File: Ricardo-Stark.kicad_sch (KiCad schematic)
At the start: 49 parts, among them J1 RBUS, U1 ESP32-S3, Y1 R940000171

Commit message: Commit
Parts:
- removed ArcReactorCore1, Eye1, Eye2: Blue_LED, Resistor_SMD:R_0402_1005Metric, symbol Device:LED_Small
- removed R11, R12, R13: 1k, Resistor_SMD:R_0402_1005Metric, symbol Device:R_Small
- removed R14: 3k, Resistor_SMD:R_0402_1005Metric, symbol Device:R_Small
- removed Repulsor1, Repulsor2: White_LED, Resistor_SMD:R_0402_1005Metric, symbol Device:LED_Small
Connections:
- net BUCKC_EN: no longer U1.17 (GPIO12/ADC2_CH1)
- net VSPI_MISO: now also U1.44 (MTCK/JTAG/GPIO39); no longer U1.21 (GPIO15/ADC2_CH4/XTAL_32K_P)
- net VSPI_MOSI: now also U1.47 (MTDI/JTAG/GPIO41); no longer U1.45 (MTDO/JTAG/GPIO40)
- net VSPI_SCLK: now also U1.45 (MTDO/JTAG/GPIO40); no longer U1.47 (MTDI/JTAG/GPIO41)
- net GPIO0 renamed GPIO9
- net GPIO1 renamed GPIO7
- net GPIO2 renamed GPIO8
- net GPIO3 renamed GPIO6
- no-connect marks 17 -> 18
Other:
- sheet actuators ports: added GPIO4, GPIO5, GPIO6, GPIO7, GPIO8, GPIO9; removed none
- sheet microSD ports: added SD1_CS, VSPI_MISO, VSPI_MOSI, VSPI_SCLK; removed none

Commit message: commit
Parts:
- added 3V3LED10: PURPLE_LED, LED_SMD:LED_0402_1005Metric, symbol Device:LED_Small
- added 3V3LED2, 3V3LED3, 3V3LED4, 3V3LED8: BLUE_LED, LED_SMD:LED_0402_1005Metric, symbol Device:LED_Small
- added 3V3LED5: ORANGE_LED, LED_SMD:LED_0402_1005Metric, symbol Device:LED_Small
- added 3V3LED6: RED_LED, LED_SMD:LED_0402_1005Metric, symbol Device:LED_Small
- added 3V3LED7: YELLOW_LED, LED_SMD:LED_0402_1005Metric, symbol Device:LED_Small
- added 3V3LED9: GREEN_LED, LED_SMD:LED_0402_1005Metric, symbol Device:LED_Small
- added JP31: SolderJumper_2_Open, iclr:SmallerSolderJP, symbol Jumper:SolderJumper_2_Open
- added R11, R12, R13, R44: 470, Resistor_SMD:R_0402_1005Metric, symbol Device:R_Small
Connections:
- net +3V3: now also JP31.2 (B), R11.2, R12.2, R44.2
- net GND: now also 3V3LED10.1 (K), 3V3LED2.1 (K), 3V3LED3.1 (K), 3V3LED4.1 (K), 3V3LED5.1 (K), 3V3LED6.1 (K), 3V3LED7.1 (K), 3V3LED8.1 (K), 3V3LED9.1 (K)
- net Servo1PWM: now also U1.17 (GPIO12/ADC2_CH1); no longer U1.16 (GPIO11/ADC2_CH0)
- net Servo2PWM: now also U1.16 (GPIO11/ADC2_CH0); no longer U1.15 (GPIO10/ADC1_CH9)
- net SD_EN: now reaches U1.43 (GPIO38)
- new net: 3V3LED10.2 (A), 3V3LED4.2 (A), 3V3LED5.2 (A), 3V3LED6.2 (A), 3V3LED7.2 (A), 3V3LED9.2 (A), JP31.1 (A), R13.1
- new net: 3V3LED2.2 (A), R11.1
- new net: 3V3LED8.2 (A), R44.1
- new net: 3V3LED3.2 (A), R12.1
- new net LEDC: R13.2, U1.15 (GPIO10/ADC1_CH9)
- no-connect marks 18 -> 16
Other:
- sheet microSD ports: added SD_Pow; removed none

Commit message: 5v breakout
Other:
- sheet actuators ports: added 5V; removed none
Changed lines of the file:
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@@
 	(wire
 		(pts
-			(xy 213.36 58.42) (xy 219.71 58.42)
+			(xy 218.44 58.42) (xy 224.79 58.42)
 		)
 		(stroke
@@
 	(wire
 		(pts
-			(xy 213.36 54.61) (xy 219.71 54.61)
+			(xy 218.44 54.61) (xy 224.79 54.61)
 		)
 		(stroke
@@
 	(wire
 		(pts
+			(xy 187.96 64.008) (xy 180.34 64.008)
+		)
+		(stroke
+			(width 0)
+			(type default)
+		)
+	)
+	(wire
+		(pts
 			(xy 55.88 127) (xy 69.85 127)
 		)
@@
 	(wire
 		(pts
-			(xy 213.36 62.23) (xy 219.71 62.23)
+			(xy 218.44 62.23) (xy 224.79 62.23)
 		)
 		(stroke
@@
 	)
 	(label "Servo1PWM"
-		(at 219.71 58.42 0)
+		(at 224.79 58.42 0)
 		(fields_autoplaced yes)
 		(effects
@@
 	)
 	(label "GPIO7"
-		(at 182.88 53.848 180)
+		(at 187.96 53.848 180)
 		(fields_autoplaced yes)
 		(effects
@@
 	)
 	(label "GPIO6"
-		(at 182.88 51.562 180)
+		(at 187.96 51.562 180)
 		(fields_autoplaced yes)
 		(effects
@@
 	)
 	(label "Servo2PWM"
-		(at 219.71 54.61 0)
+		(at 224.79 54.61 0)
 		(fields_autoplaced yes)
 		(effects
@@
 	)
 	(label "GPIO9"
-		(at 182.88 62.484 180)
+		(at 187.96 62.484 180)
 		(fields_autoplaced yes)
 		(effects
@@
 	)
 	(label "GPIO4"
-		(at 182.88 56.134 180)
+		(at 187.96 56.134 180)
 		(fields_autoplaced yes)
 		(effects
@@
 	)
 	(label "ServoV_LOG"
-		(at 219.71 62.23 0)
+		(at 224.79 62.23 0)
 		(fields_autoplaced yes)
 		(effects
@@
 	)
 	(label "GPIO8"
-		(at 182.88 60.452 180)
+		(at 187.96 60.452 180)
 		(fields_autoplaced yes)
 		(effects
@@
 	)
 	(label "GPIO5"
-		(at 182.88 58.166 180)
+		(at 187.96 58.166 180)
 		(fields_autoplaced yes)
 		(effects
@@
 	)
 	(symbol
+		(lib_id "power:+5V")
+		(at 180.34 64.008 180)
+		(unit 1)
+		(exclude_from_sim no)
+		(in_bom yes)
+		(on_board yes)
+		(dnp no)
+		(fields_autoplaced yes)
+		(property "Reference" "#PWR092"
+			(at 180.34 60.198 0)
+			(effects
+				(font
+					(size 1.27 1.27)
+				)
+				(hide yes)
+			)
+		)
+		(property "Value" "+5V"
+			(at 180.34 69.088 0)
+			(effects
+				(font
+					(size 1.27 1.27)
+				)
+			)
+		)
+		(property "Footprint" ""
+			(at 180.34 64.008 0)
+			(effects
+				(font
+					(size 1.27 1.27)
+				)
+				(hide yes)
+			)
+		)
+		(property "Datasheet" ""
+			(at 180.34 64.008 0)
+			(effects
+				(font
+					(size 1.27 1.27)
+				)
+				(hide yes)
+			)
+		)
+		(property "Description" ""
+			(at 180.34 64.008 0)
+			(effects
+				(font
+					(size 1.27 1.27)
+				)
+				(hide yes)
+			)
+		)
+		(pin "1"
+		)
+		(instances
+			(project "Ricardo-Stark"
+				(path "/7db990e4-92e1-4f99-b4d2-435bbec1ba83"
+					(reference "#PWR092")
+					(unit 1)
+				)
+			)
+		)
+	)
+	(symbol
 		(lib_id "power:+3.3V")
 		(at 59.69 142.24 0)
@@
 	)
 	(sheet
-		(at 182.88 49.53)
+		(at 187.96 49.53)
 		(size 30.48 15.24)
 		(fields_autoplaced yes)
@@
 		)
 		(property "Sheetname" "actuators"
-			(at 182.88 48.8184 0)
+			(at 187.96 48.8184 0)
 			(effects
 				(font
@@
 		)
 		(property "Sheetfile" "actuators.kicad_sch"
-			(at 182.88 65.3546 0)
+			(at 187.96 65.3546 0)
 			(effects
 				(font
@@
 		)
 		(pin "SERVO2" bidirectional
-			(at 213.36 54.61 0)
+			(at 218.44 54.61 0)
 			(effects
 				(font
@@
 		)
 		(pin "SERVO1" bidirectional
-			(at 213.36 58.42 0)
+			(at 218.44 58.42 0)
 			(effects
 				(font
@@
 		)
 		(pin "SERVO_LOG" output
-			(at 213.36 62.23 0)
+			(at 218.44 62.23 0)
 			(effects
 				(font
@@
 		)
 		(pin "GPIO6" input
-			(at 182.88 51.562 180)
+			(at 187.96 51.562 180)
 			(effects
 				(font
@@
 		)
 		(pin "GPIO7" input
-			(at 182.88 53.848 180)
+			(at 187.96 53.848 180)
 			(effects
 				(font
@@
 		)
 		(pin "GPIO4" input
-			(at 182.88 56.134 180)
+			(at 187.96 56.134 180)
 			(effects
 				(font
@@
 		)
 		(pin "GPIO5" input
-			(at 182.88 58.166 180)
+			(at 187.96 58.166 180)
 			(effects
 				(font
@@
 		)
 		(pin "GPIO8" input
-			(at 182.88 60.452 180)
+			(at 187.96 60.452 180)
 			(effects
 				(font
@@
 		)
 		(pin "GPIO9" input
-			(at 182.88 62.484 180)
+			(at 187.96 62.484 180)
+			(effects
+				(font
+					(size 1.27 1.27)
+				)
+				(justify left)
+			)
+		)
+		(pin "5V" output
+			(at 187.96 64.008 180)
 			(effects
 				(font

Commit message: review changes
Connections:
- net Fuse_Cont: now reaches U1.19 (GPIO14/ADC2_CH3)
- no-connect marks 16 -> 15
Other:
- sheet Pyro ports: added Fuse_Cont; removed none
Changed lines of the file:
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@@
 	)
 	(no_connect
-		(at 69.85 105.41)
-	)
-	(no_connect
 		(at 135.89 87.63)
 	)
@@
 	(wire
 		(pts
+			(xy 207.264 134.874) (xy 214.884 134.874)
+		)
+		(stroke
+			(width 0)
+			(type default)
+		)
+	)
+	(wire
+		(pts
 			(xy 143.51 138.43) (xy 156.21 138.43)
 		)
@@
 		)
 	)
+	(label "Fuse_Cont"
+		(at 69.85 105.41 180)
+		(fields_autoplaced yes)
+		(effects
+			(font
+				(size 1.27 1.27)
+			)
+			(justify right bottom)
+		)
+	)
 	(label "VSPI_MISO"
 		(at 69.85 118.11 180)
@@
 		)
 	)
+	(label "Fuse_Cont"
+		(at 207.264 134.874 180)
+		(fields_autoplaced yes)
+		(effects
+			(font
+				(size 1.27 1.27)
+			)
+			(justify right bottom)
+		)
+	)
 	(label "CAN-"
 		(at 115.57 25.4 270)
@@
 			(effects
 				(font
+					(size 1.27 1.27)
+				)
+				(justify left)
+			)
+		)
+		(pin "Fuse_Cont" output
+			(at 214.884 134.874 180)
+			(effects
+				(font

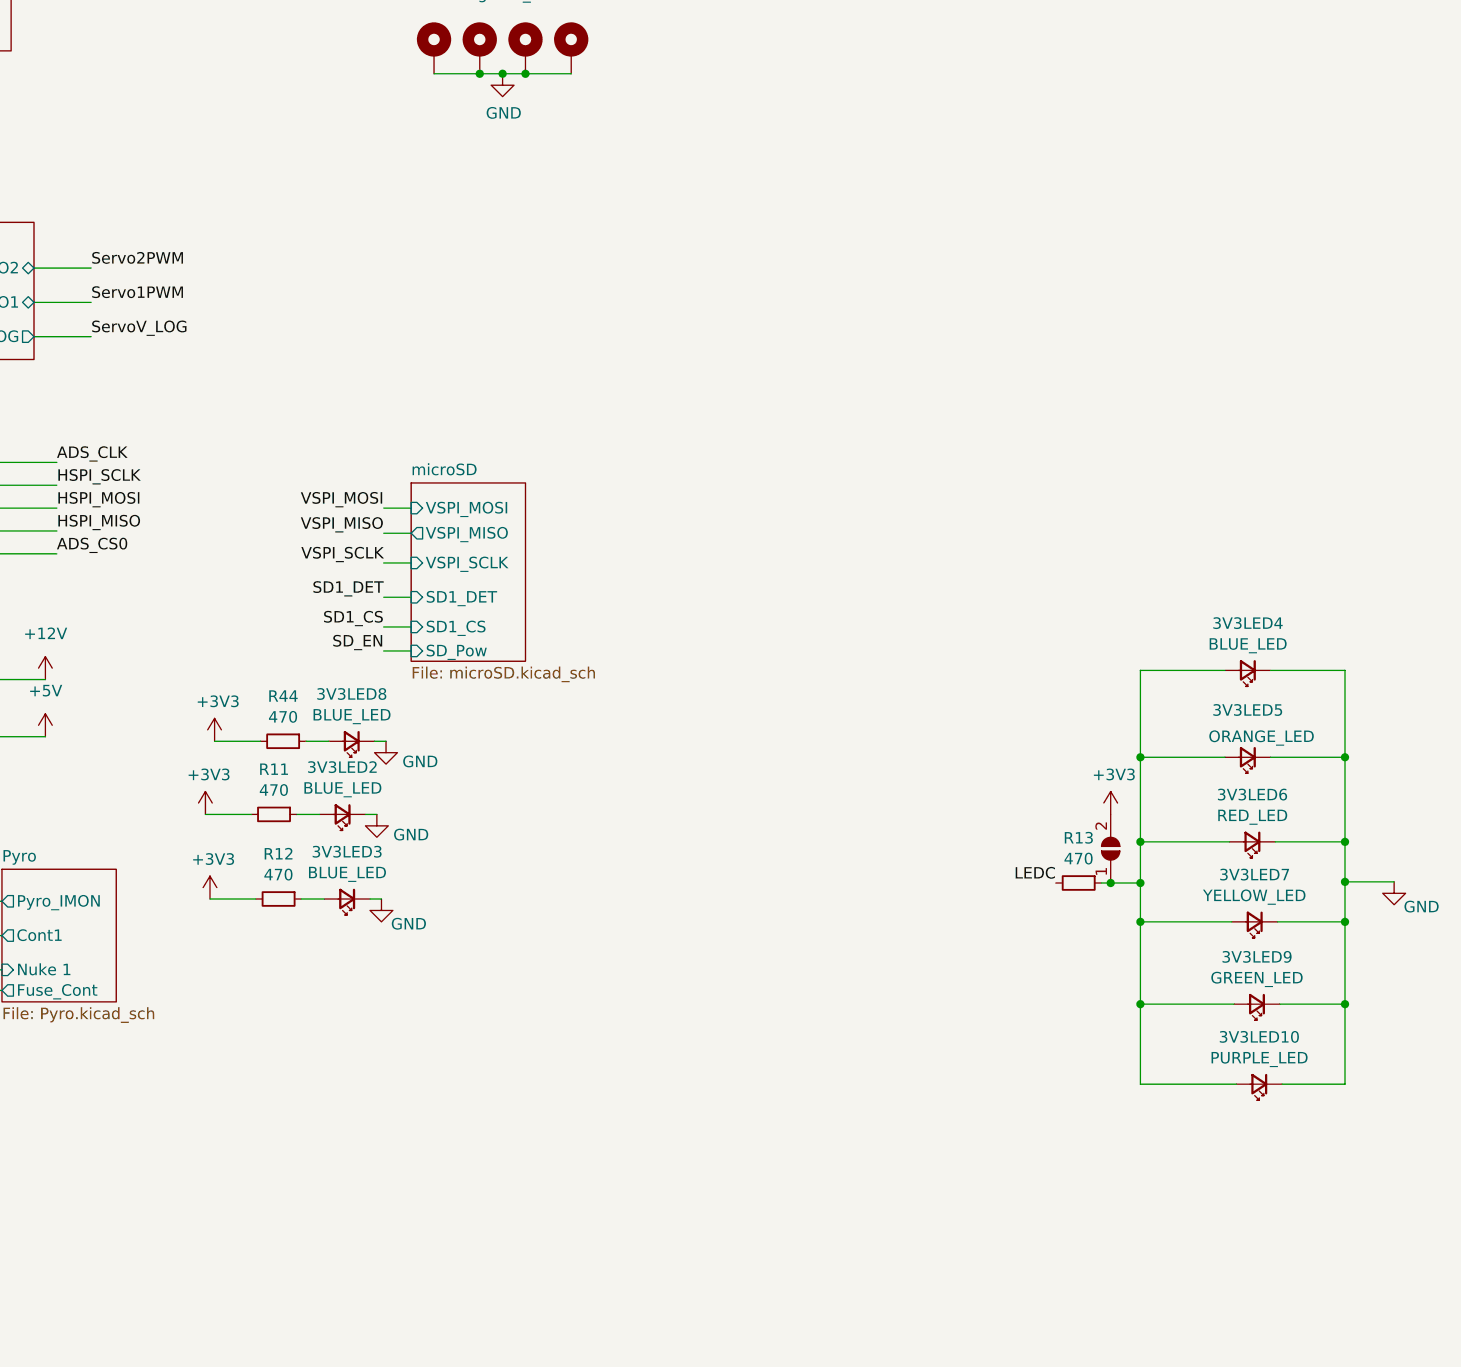
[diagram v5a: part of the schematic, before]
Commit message: saved leds from blowing
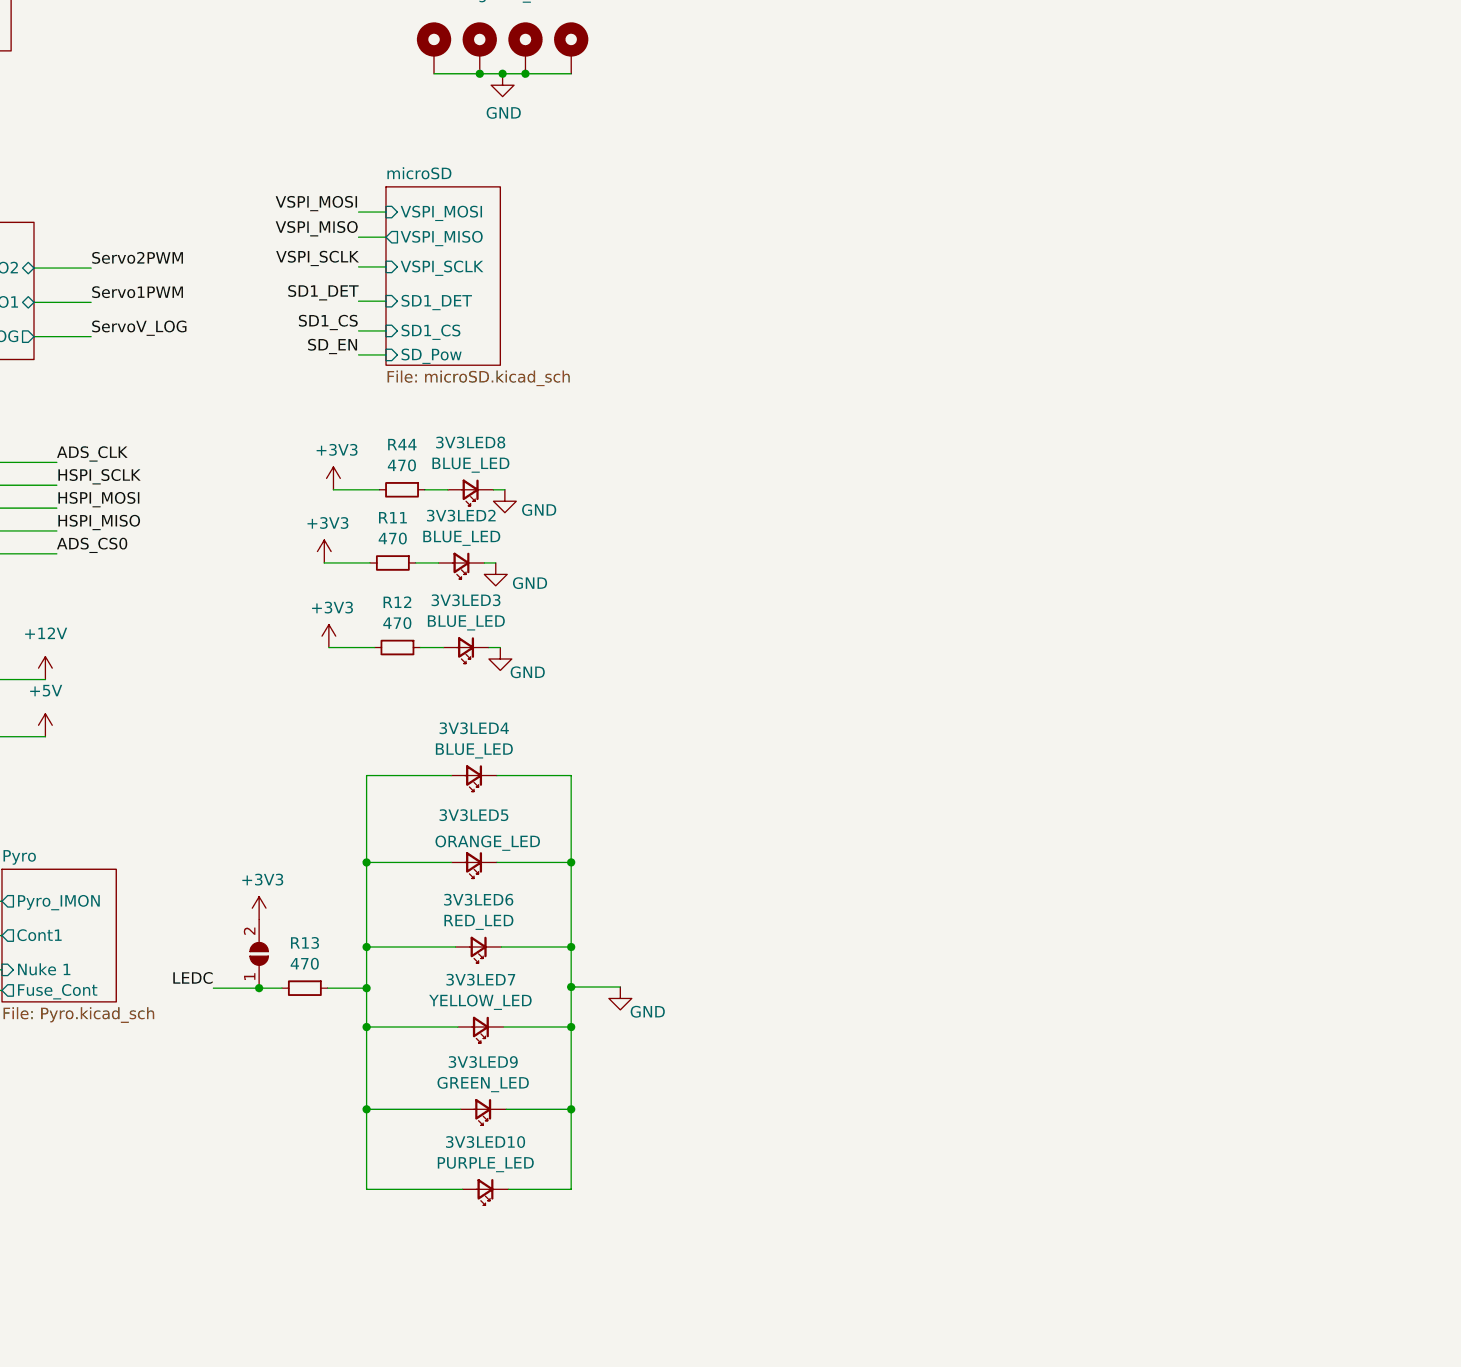
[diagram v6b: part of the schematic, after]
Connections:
- net LEDC: now also JP31.1 (A)
- net at 3V3LED10.2 (A), 3V3LED4.2 (A), 3V3LED5.2 (A)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: no longer JP31.1 (A)
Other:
- moved on the sheet: 3V3LED10, 3V3LED2, 3V3LED3, 3V3LED4, 3V3LED5, 3V3LED6, 3V3LED7, 3V3LED8, 3V3LED9, R11, R12, R13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
